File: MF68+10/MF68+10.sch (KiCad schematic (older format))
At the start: 164 parts, among them U1 Teensy_3.2, U2 AN32183A

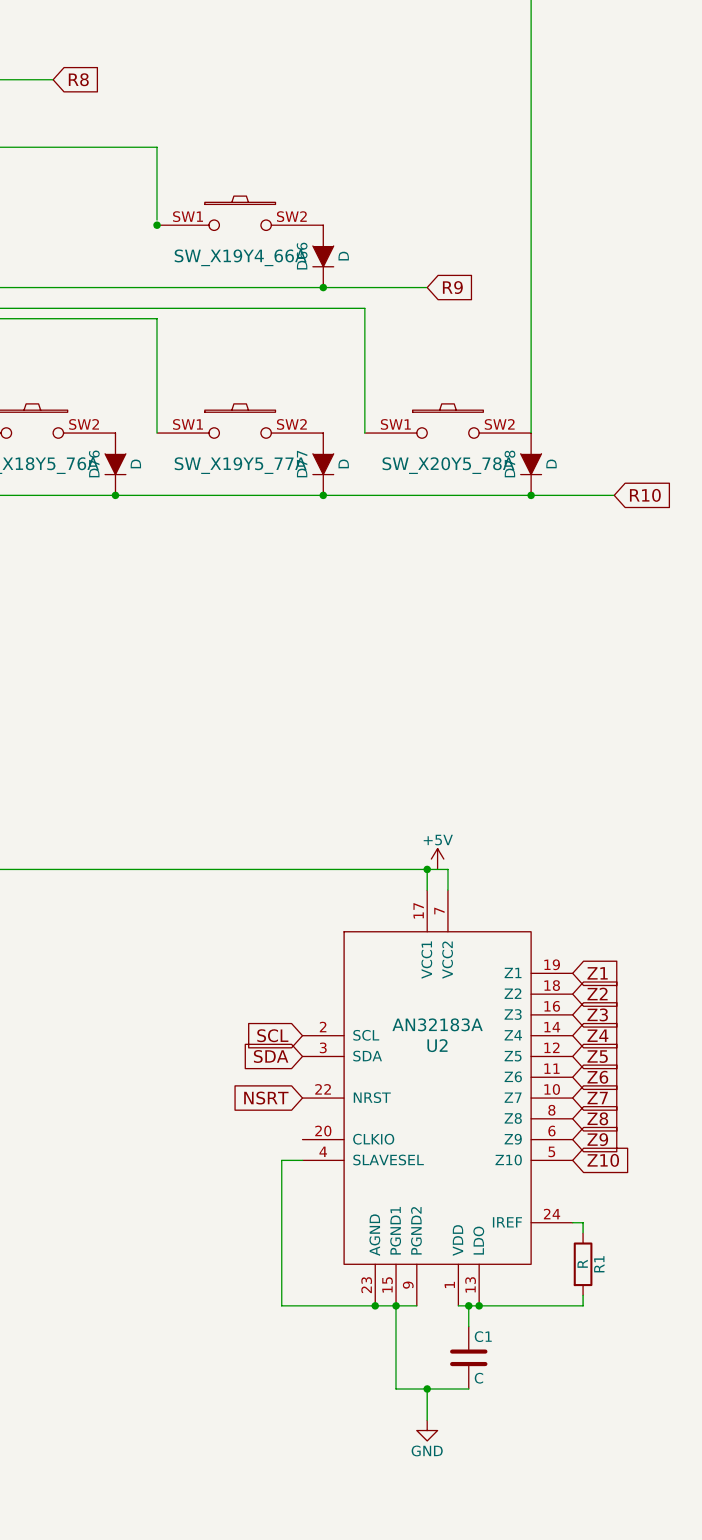
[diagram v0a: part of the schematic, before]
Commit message: Added PCB stabilizers to both 103 key and MF68+10
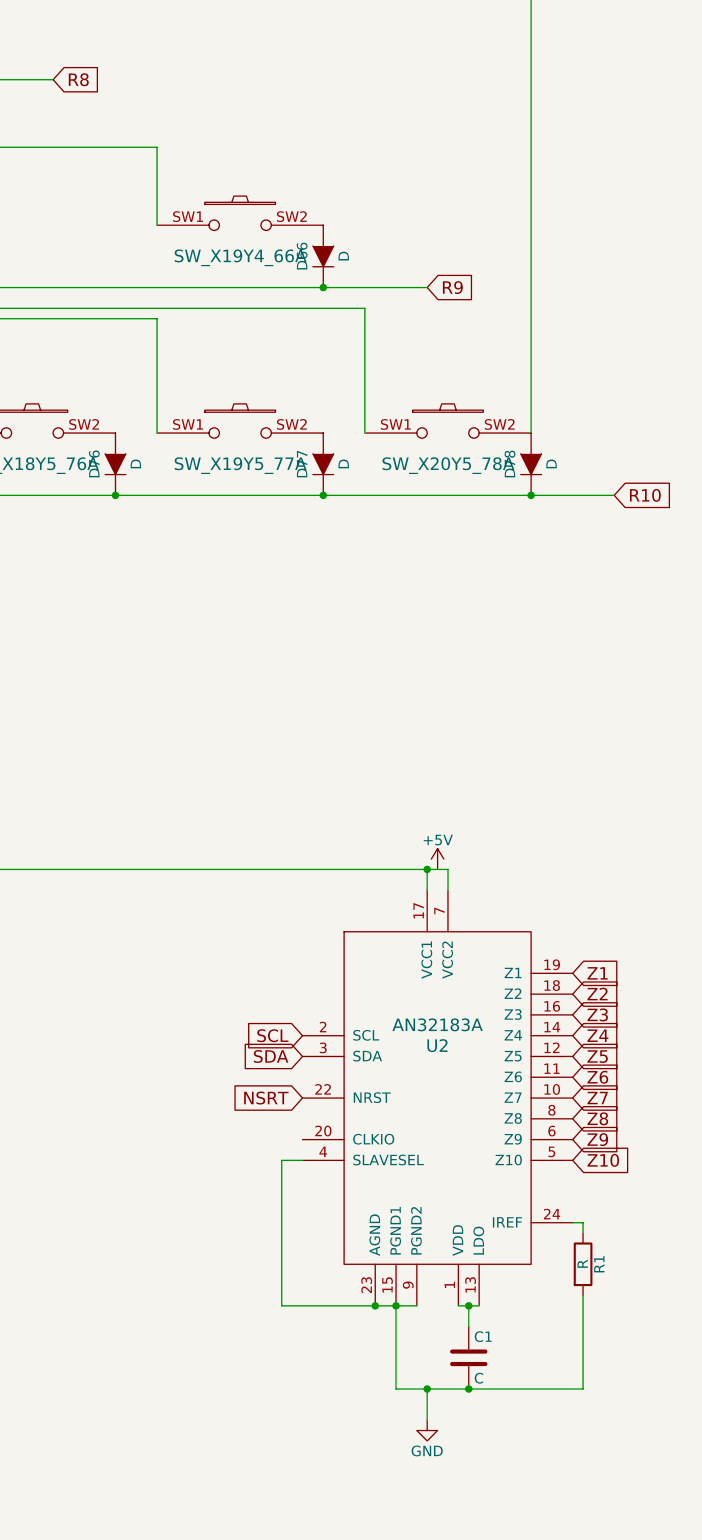
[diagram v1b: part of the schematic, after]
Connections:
- net C7: now also SW_X19Y4_66.SW1
- net GND: now also R1.2
- net at C1.1, U2.1 (VDD), U2.13 (LDO): no longer R1.2
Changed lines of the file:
@@
 Connection ~ 12200 4600
 Connection ~ 13200 4600
-Connection ~ 19200 4600
 Connection ~ 14200 4600
 Wire Wire Line
@@
 Wire Wire Line
 	17325 4225 19200 4225
-Wire Wire Line
-	19200 4225 19200 4575
 Wire Wire Line
 	21000 2900 21000 5600
@@
 $EndComp
 Wire Wire Line
-	20350 10200 20700 10200
+	20350 10200 21250 10200
 Wire Wire Line
 	20500 10200 20500 10350
@@
 $EndComp
 Wire Wire Line
-	21250 9800 21250 9750
+	21250 10200 21250 9750
 $Comp
 L AN32183A U2
@@
 	21250 9400 21250 9450
 Wire Wire Line
-	20650 9800 21250 9800
-Wire Wire Line
 	20700 9800 20700 9900
-Connection ~ 20700 9800
-Connection ~ 20750 9800
 Connection ~ 15800 7700
 Connection ~ 20500 7700
@@
 	1    0    0    -1
 $EndComp
+Wire Wire Line
+	19200 4225 19200 4600
+Connection ~ 20700 10200
+Wire Wire Line
+	20650 9800 20750 9800
+Connection ~ 20700 9800
 $EndSCHEMATC

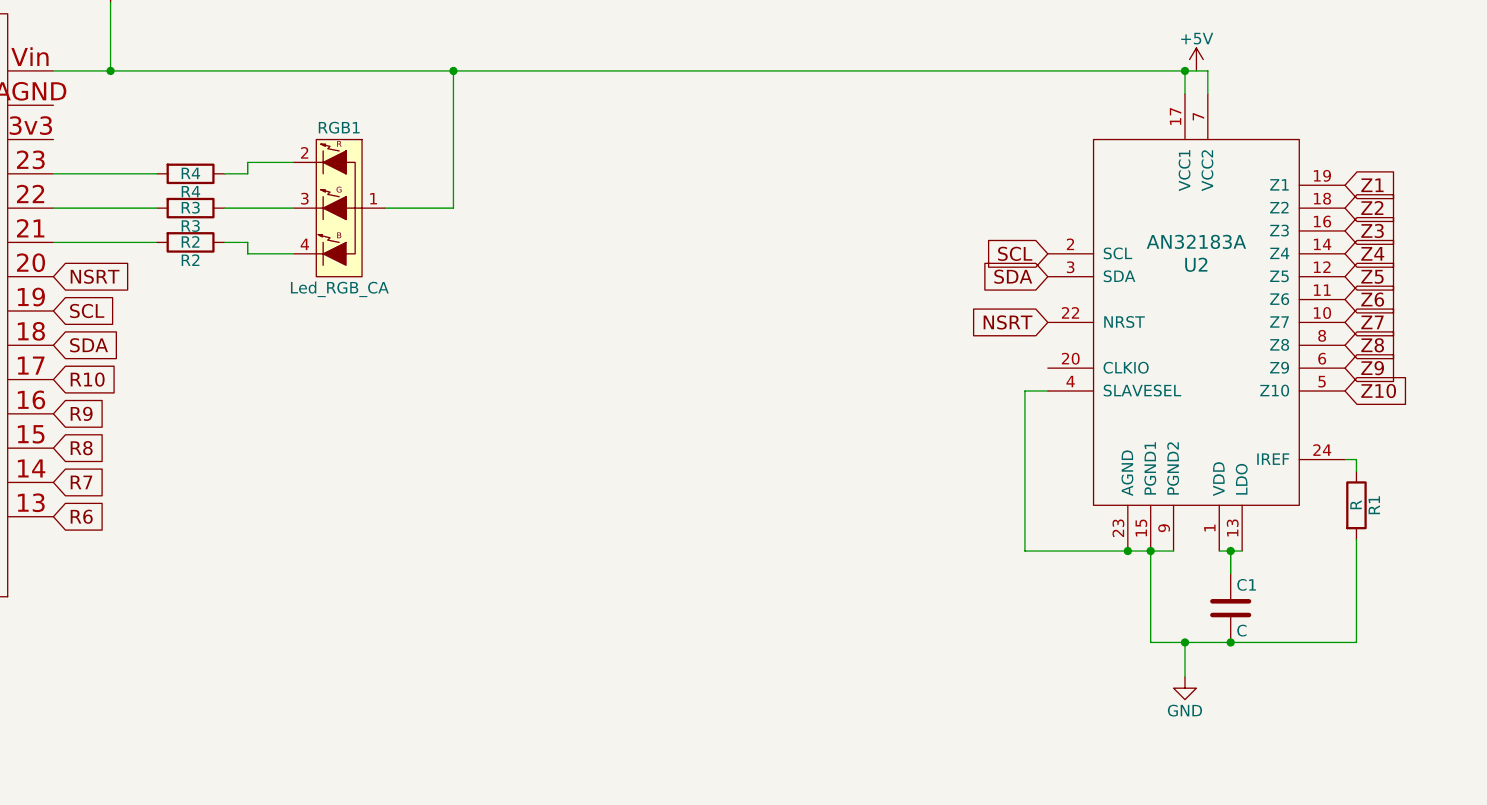
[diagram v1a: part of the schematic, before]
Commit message: Renamed BlueWeevil to LFK78
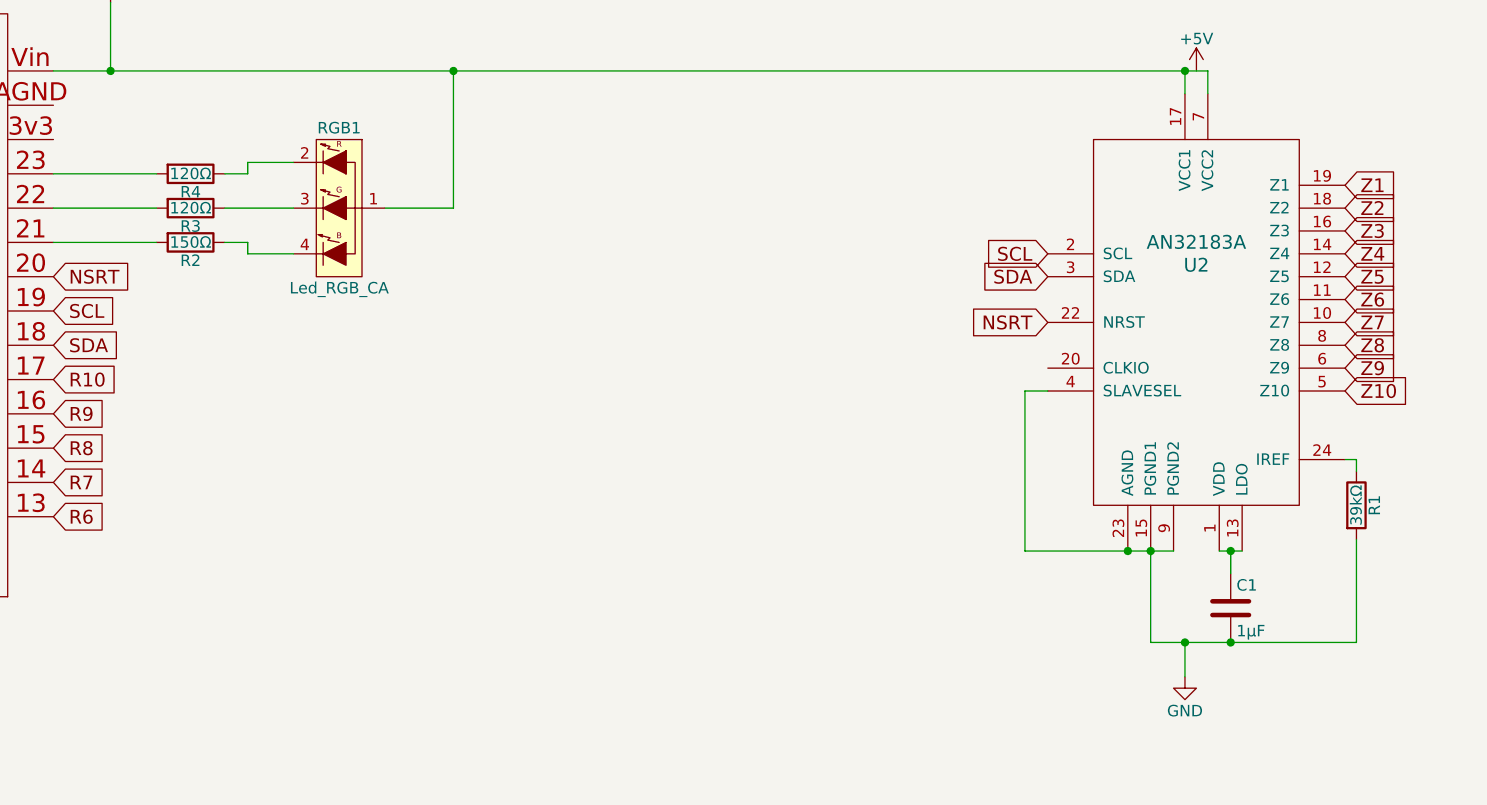
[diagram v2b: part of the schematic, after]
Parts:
- C1: value C -> 1µF
- R1: value R -> 39kΩ
- R2: value R2 -> 150Ω
- R3: value R3 -> 120Ω
- R4: value R4 -> 120Ω
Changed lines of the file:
@@
 P 20700 10050
 F 0 "C1" H 20725 10150 50  0000 L CNN
-F 1 "C" H 20725 9950 50  0000 L CNN
+F 1 "1µF" H 20725 9950 50  0000 L CNN
 F 2 "Capacitors_SMD:C_1206_HandSoldering" H 20738 9900 50  0001 C CNN
 F 3 "" H 20700 10050 50  0000 C CNN
@@
 P 21250 9600
 F 0 "R1" V 21330 9600 50  0000 C CNN
-F 1 "R" V 21250 9600 50  0000 C CNN
+F 1 "39kΩ" V 21250 9600 50  0000 C CNN
 F 2 "Resistors_SMD:R_1206_HandSoldering" V 21180 9600 50  0001 C CNN
 F 3 "" H 21250 9600 50  0000 C CNN
@@
 P 16150 8450
 F 0 "R2" V 16230 8450 50  0000 C CNN
-F 1 "R2" V 16150 8450 50  0000 C CNN
+F 1 "150Ω" V 16150 8450 50  0000 C CNN
 F 2 "Resistors_SMD:R_1206_HandSoldering" V 16080 8450 50  0001 C CNN
 F 3 "" H 16150 8450 50  0000 C CNN
@@
 P 16150 8300
 F 0 "R3" V 16230 8300 50  0000 C CNN
-F 1 "R3" V 16150 8300 50  0000 C CNN
+F 1 "120Ω" V 16150 8300 50  0000 C CNN
 F 2 "Resistors_SMD:R_1206_HandSoldering" V 16080 8300 50  0001 C CNN
 F 3 "" H 16150 8300 50  0000 C CNN
@@
 P 16150 8150
 F 0 "R4" V 16230 8150 50  0000 C CNN
-F 1 "R4" V 16150 8150 50  0000 C CNN
+F 1 "120Ω" V 16150 8150 50  0000 C CNN
 F 2 "Resistors_SMD:R_1206_HandSoldering" V 16080 8150 50  0001 C CNN
 F 3 "" H 16150 8150 50  0000 C CNN
